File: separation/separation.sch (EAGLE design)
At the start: 5 parts, among them IC1 L7805ACV

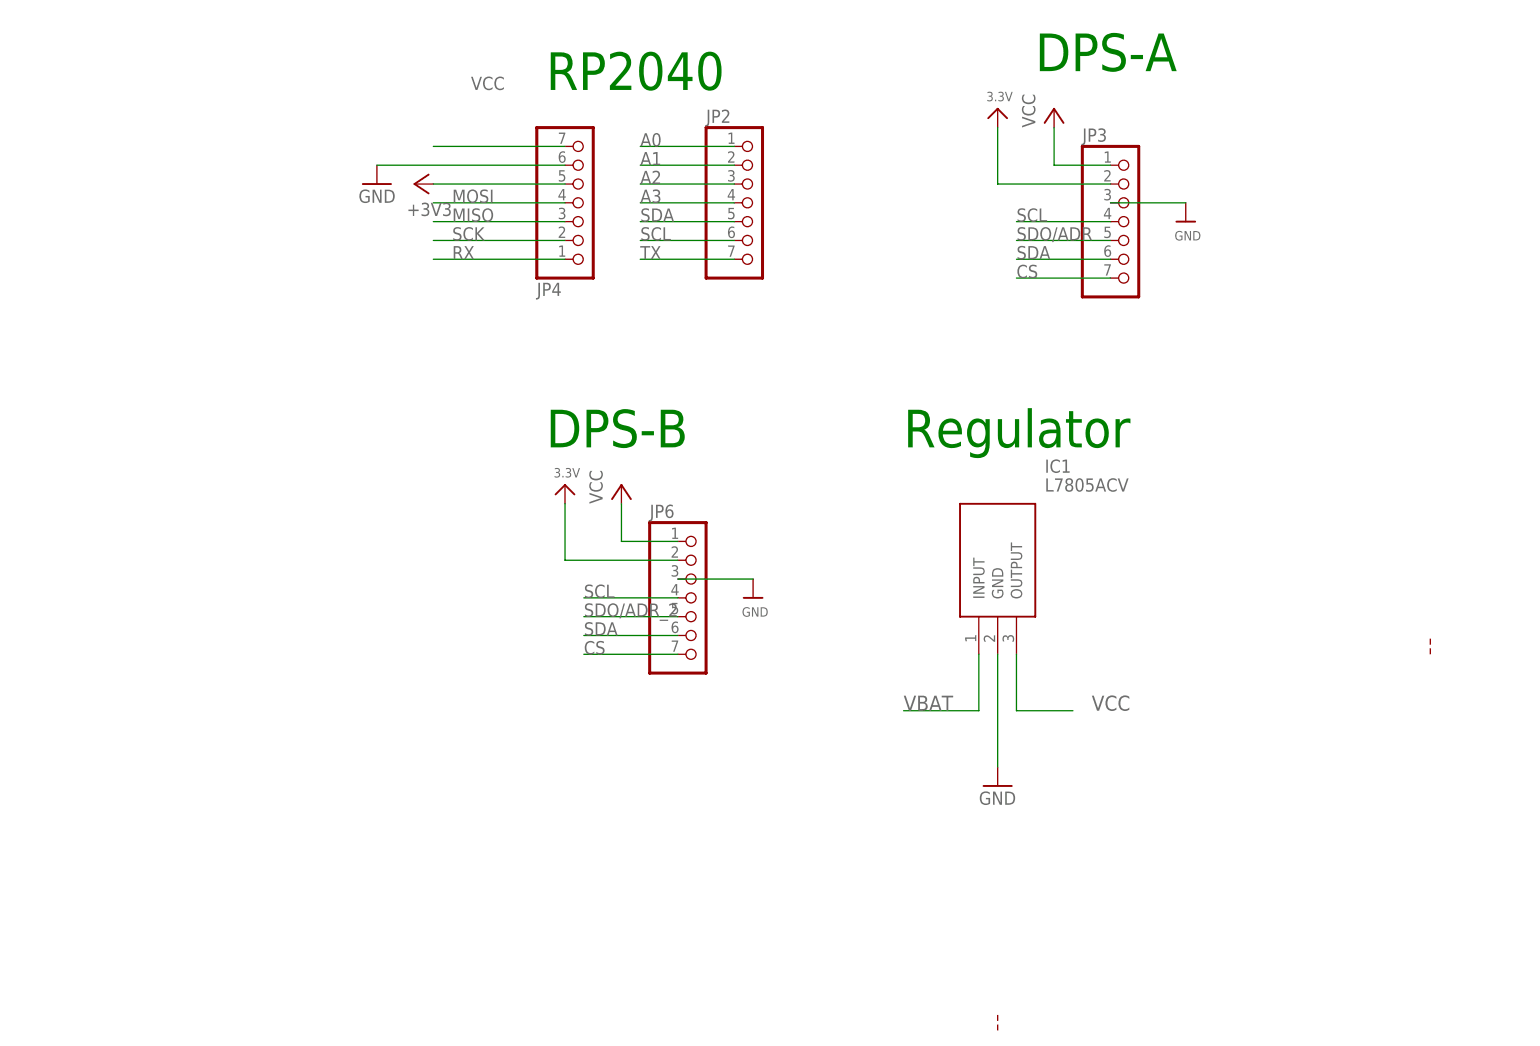
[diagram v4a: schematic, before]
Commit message: add buzzer
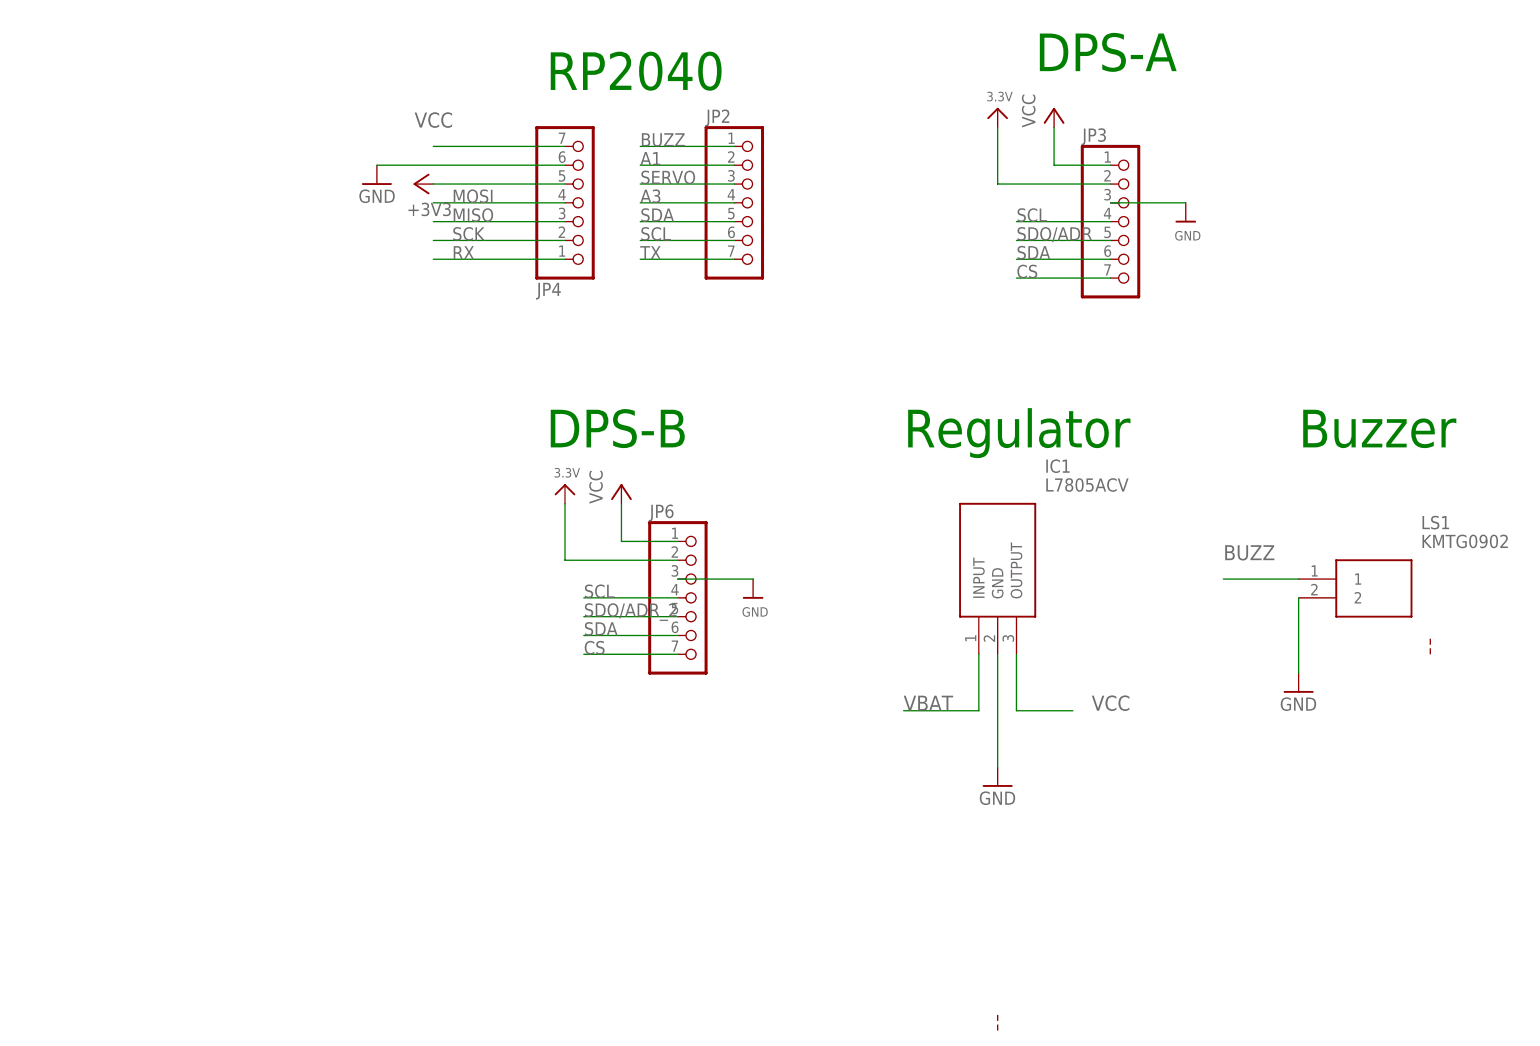
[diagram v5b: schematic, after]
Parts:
- added LS1: KMTG0902, SamacSys_Parts:KMTG0902
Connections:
- net A2 renamed SERVO
- removed net A0: JP2.1
- new net BUZZ: JP2.1, LS1.1
- net GND: now also LS1.2
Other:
- note added: "Buzzer"
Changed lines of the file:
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@@
 <part name="IC1" library="SamacSys_Parts" deviceset="L7805ACV" device=""/>
 <part name="GND2" library="supply1" library_urn="urn:adsk.eagle:library:371" deviceset="GND" device=""/>
+<part name="LS1" library="SamacSys_Parts" deviceset="KMTG0902" device=""/>
+<part name="GND3" library="supply1" library_urn="urn:adsk.eagle:library:371" deviceset="GND" device=""/>
 </parts>
 <sheets>
@@
 <wire x1="91.44" y1="-48.26" x2="91.44" y2="-45.72" width="0.1524" layer="94" style="shortdash"/>
 <text x="78.74" y="30.48" size="5.08" layer="91">Regulator</text>
+<text x="132.08" y="30.48" size="5.08" layer="91">Buzzer</text>
 </plain>
 <instances>
@@
 <attribute name="VALUE" x="88.9" y="-17.78" size="1.778" layer="96"/>
 </instance>
+<instance part="LS1" gate="G$1" x="132.08" y="12.7" smashed="yes">
+<attribute name="NAME" x="148.59" y="20.32" size="1.778" layer="95" align="center-left"/>
+<attribute name="VALUE" x="148.59" y="17.78" size="1.778" layer="96" align="center-left"/>
+</instance>
+<instance part="GND3" gate="1" x="132.08" y="-2.54" smashed="yes">
+<attribute name="VALUE" x="129.54" y="-5.08" size="1.778" layer="96"/>
+</instance>
 </instances>
 <busses>
@@
 <pinref part="GND2" gate="1" pin="GND"/>
 </segment>
+<segment>
+<pinref part="LS1" gate="G$1" pin="2"/>
+<pinref part="GND3" gate="1" pin="GND"/>
+<wire x1="132.08" y1="10.16" x2="132.08" y2="0" width="0.1524" layer="91"/>
+</segment>
 </net>
 <net name="MOSI" class="0">
@@
 </segment>
 </net>
-<net name="A2" class="0">
+<net name="SERVO" class="0">
 <segment>
 <label x="43.18" y="66.04" size="1.778" layer="95"/>
@@
 </segment>
 </net>
-<net name="A0" class="0">
-<segment>
-<label x="43.18" y="71.12" size="1.778" layer="95"/>
-<pinref part="JP2" gate="A" pin="1"/>
-<wire x1="43.18" y1="71.12" x2="55.88" y2="71.12" width="0.1524" layer="91"/>
-</segment>
-</net>
 <net name="SCL" class="0">
 <segment>
@@
 <wire x1="33.02" y1="71.12" x2="15.24" y2="71.12" width="0.1524" layer="91"/>
 <pinref part="JP4" gate="A" pin="7"/>
-<label x="20.32" y="78.74" size="1.778" layer="95"/>
+<label x="12.7" y="73.66" size="2.032" layer="95"/>
 </segment>
 <segment>
@@
 </segment>
 </net>
+<net name="BUZZ" class="0">
+<segment>
+<pinref part="LS1" gate="G$1" pin="1"/>
+<wire x1="132.08" y1="12.7" x2="121.92" y2="12.7" width="0.1524" layer="91"/>
+<label x="121.92" y="15.24" size="2.032" layer="95"/>
+</segment>
+<segment>
+<label x="43.18" y="71.12" size="1.778" layer="95"/>
+<pinref part="JP2" gate="A" pin="1"/>
+<wire x1="43.18" y1="71.12" x2="55.88" y2="71.12" width="0.1524" layer="91"/>
+</segment>
+</net>

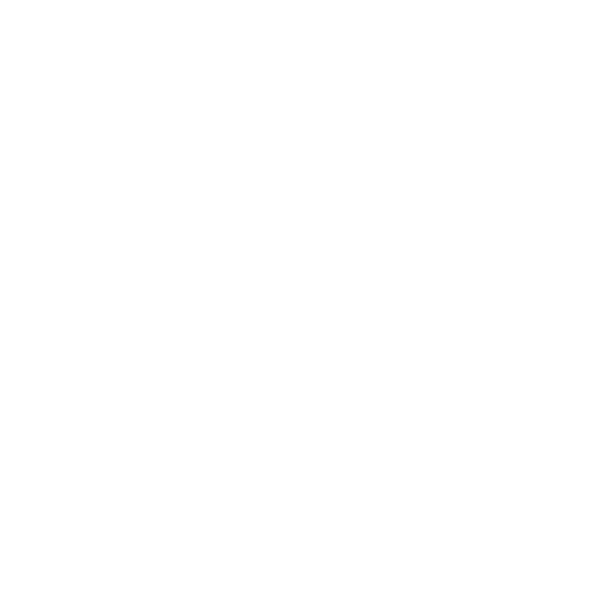
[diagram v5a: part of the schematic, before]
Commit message: add servo connection
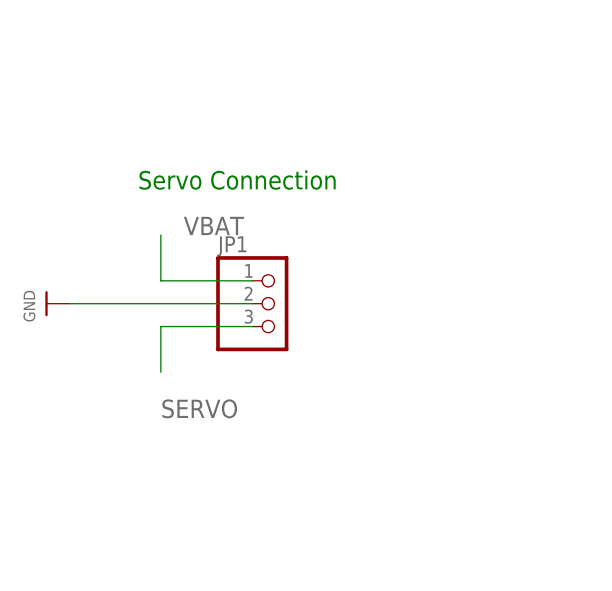
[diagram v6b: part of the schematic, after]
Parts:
- added JP1: (no value), pinhead:PINHD-1X3
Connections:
- net GND: now also JP1.2
- net SERVO: now also JP1.3
- net VBAT: now also JP1.1
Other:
- note added: "Servo Connection"
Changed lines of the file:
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@@
 <part name="LS1" library="SamacSys_Parts" deviceset="KMTG0902" device=""/>
 <part name="GND3" library="supply1" library_urn="urn:adsk.eagle:library:371" deviceset="GND" device=""/>
+<part name="JP1" library="pinhead" library_urn="urn:adsk.eagle:library:325" deviceset="PINHD-1X3" device="" package3d_urn="urn:adsk.eagle:package:22458/2"/>
+<part name="U$3" library="microbuilder" deviceset="GND" device=""/>
 </parts>
 <sheets>
@@
 <text x="78.74" y="30.48" size="5.08" layer="91">Regulator</text>
 <text x="132.08" y="30.48" size="5.08" layer="91">Buzzer</text>
+<text x="-27.94" y="25.4" size="2.032" layer="91">Servo Connection</text>
 </plain>
 <instances>
@@
 <attribute name="VALUE" x="129.54" y="-5.08" size="1.778" layer="96"/>
 </instance>
+<instance part="JP1" gate="A" x="-12.7" y="12.7" smashed="yes">
+<attribute name="NAME" x="-19.05" y="18.415" size="1.778" layer="95"/>
+<attribute name="VALUE" x="-19.05" y="5.08" size="1.778" layer="96"/>
+</instance>
+<instance part="U$3" gate="G$1" x="-38.1" y="12.7" smashed="yes" rot="R270">
+<attribute name="VALUE" x="-40.64" y="14.224" size="1.27" layer="96" rot="R270"/>
+</instance>
 </instances>
 <busses>
@@
 <wire x1="132.08" y1="10.16" x2="132.08" y2="0" width="0.1524" layer="91"/>
 </segment>
+<segment>
+<pinref part="JP1" gate="A" pin="2"/>
+<wire x1="-15.24" y1="12.7" x2="-35.56" y2="12.7" width="0.1524" layer="91"/>
+<pinref part="U$3" gate="G$1" pin="GND"/>
+</segment>
 </net>
 <net name="MOSI" class="0">
@@
 <pinref part="JP2" gate="A" pin="3"/>
 <wire x1="43.18" y1="66.04" x2="55.88" y2="66.04" width="0.1524" layer="91"/>
+</segment>
+<segment>
+<pinref part="JP1" gate="A" pin="3"/>
+<wire x1="-15.24" y1="10.16" x2="-25.4" y2="10.16" width="0.1524" layer="91"/>
+<wire x1="-25.4" y1="10.16" x2="-25.4" y2="5.08" width="0.1524" layer="91"/>
+<label x="-25.4" y="0" size="2.032" layer="95"/>
 </segment>
 </net>
@@
 <wire x1="88.9" y1="-5.08" x2="78.74" y2="-5.08" width="0.1524" layer="91"/>
 <label x="78.74" y="-5.08" size="2.032" layer="95"/>
+</segment>
+<segment>
+<pinref part="JP1" gate="A" pin="1"/>
+<wire x1="-15.24" y1="15.24" x2="-25.4" y2="15.24" width="0.1524" layer="91"/>
+<wire x1="-25.4" y1="15.24" x2="-25.4" y2="20.32" width="0.1524" layer="91"/>
+<label x="-22.86" y="20.32" size="2.032" layer="95"/>
 </segment>
 </net>
@@
 will not be understood (or retained) with this version.
 </note>
+<note version="8.3" severity="warning">
+Since Version 8.3, EAGLE supports the association of 3D packages
+with devices in libraries, schematics, and board files. Those 3D
+packages will not be understood (or retained) with this version.
+</note>
 </compatibility>

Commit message: basic board layout
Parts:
- added PAD1, PAD2: WIREPAD3,17/1,1, wirepad:WIREPAD3,17/1,1
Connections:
- net GND: now also PAD2.P
- net VBAT: now also PAD1.P
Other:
- note added: "Battery Connection"
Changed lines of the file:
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@@
 <part name="JP1" library="pinhead" library_urn="urn:adsk.eagle:library:325" deviceset="PINHD-1X3" device="" package3d_urn="urn:adsk.eagle:package:22458/2"/>
 <part name="U$3" library="microbuilder" deviceset="GND" device=""/>
+<part name="PAD1" library="wirepad" library_urn="urn:adsk.eagle:library:412" deviceset="WIREPAD" device="3,17/1,1" package3d_urn="urn:adsk.eagle:package:30832/1"/>
+<part name="PAD2" library="wirepad" library_urn="urn:adsk.eagle:library:412" deviceset="WIREPAD" device="3,17/1,1" package3d_urn="urn:adsk.eagle:package:30832/1"/>
+<part name="U$4" library="microbuilder" deviceset="GND" device=""/>
 </parts>
 <sheets>
@@
 <text x="132.08" y="30.48" size="5.08" layer="91">Buzzer</text>
 <text x="-27.94" y="25.4" size="2.032" layer="91">Servo Connection</text>
+<text x="7.62" y="-12.7" size="2.032" layer="91">Battery Connection</text>
 </plain>
 <instances>
@@
 <attribute name="VALUE" x="-40.64" y="14.224" size="1.27" layer="96" rot="R270"/>
 </instance>
+<instance part="PAD1" gate="G$1" x="2.54" y="-20.32" smashed="yes">
+<attribute name="NAME" x="1.397" y="-18.4658" size="1.778" layer="95"/>
+<attribute name="VALUE" x="1.397" y="-23.622" size="1.778" layer="96"/>
+</instance>
+<instance part="PAD2" gate="G$1" x="2.54" y="-30.48" smashed="yes">
+<attribute name="NAME" x="1.397" y="-28.6258" size="1.778" layer="95"/>
+<attribute name="VALUE" x="1.397" y="-33.782" size="1.778" layer="96"/>
+</instance>
+<instance part="U$4" gate="G$1" x="25.4" y="-30.48" smashed="yes" rot="R90">
+<attribute name="VALUE" x="27.94" y="-32.004" size="1.27" layer="96" rot="R90"/>
+</instance>
 </instances>
 <busses>
@@
 <pinref part="U$3" gate="G$1" pin="GND"/>
 </segment>
+<segment>
+<pinref part="PAD2" gate="G$1" pin="P"/>
+<pinref part="U$4" gate="G$1" pin="GND"/>
+<wire x1="5.08" y1="-30.48" x2="22.86" y2="-30.48" width="0.1524" layer="91"/>
+</segment>
 </net>
 <net name="MOSI" class="0">
@@
 <label x="-22.86" y="20.32" size="2.032" layer="95"/>
 </segment>
-</net>
+<segment>
+<pinref part="PAD1" gate="G$1" pin="P"/>
+<wire x1="5.08" y1="-20.32" x2="27.94" y2="-20.32" width="0.1524" layer="91"/>
+<label x="33.02" y="-20.32" size="2.032" layer="95"/>
+</segment>
+</net>
